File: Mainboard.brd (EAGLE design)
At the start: 162.6 x 52.1 mm, 77 parts, among them IC1 MS5611-01BA03, IC2 MCP73831, Q1 BSS84, U1 LM2937IMP-3.3, U2 USD-SOCKETNEW

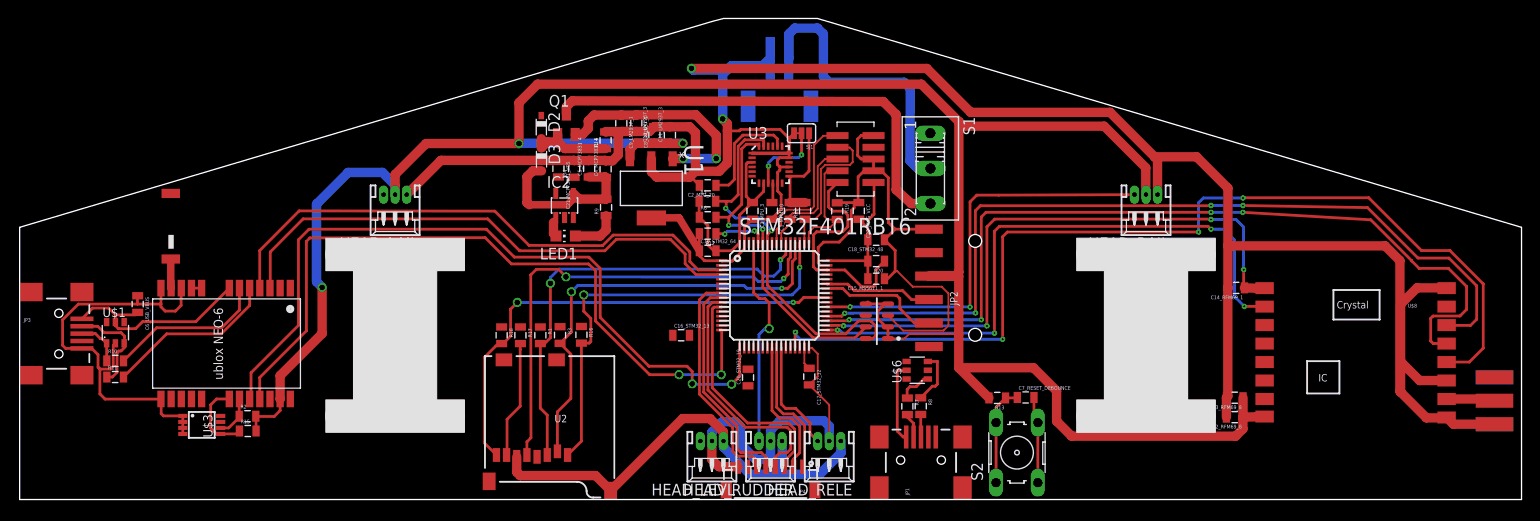
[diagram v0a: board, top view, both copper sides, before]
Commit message: Updated board wiring
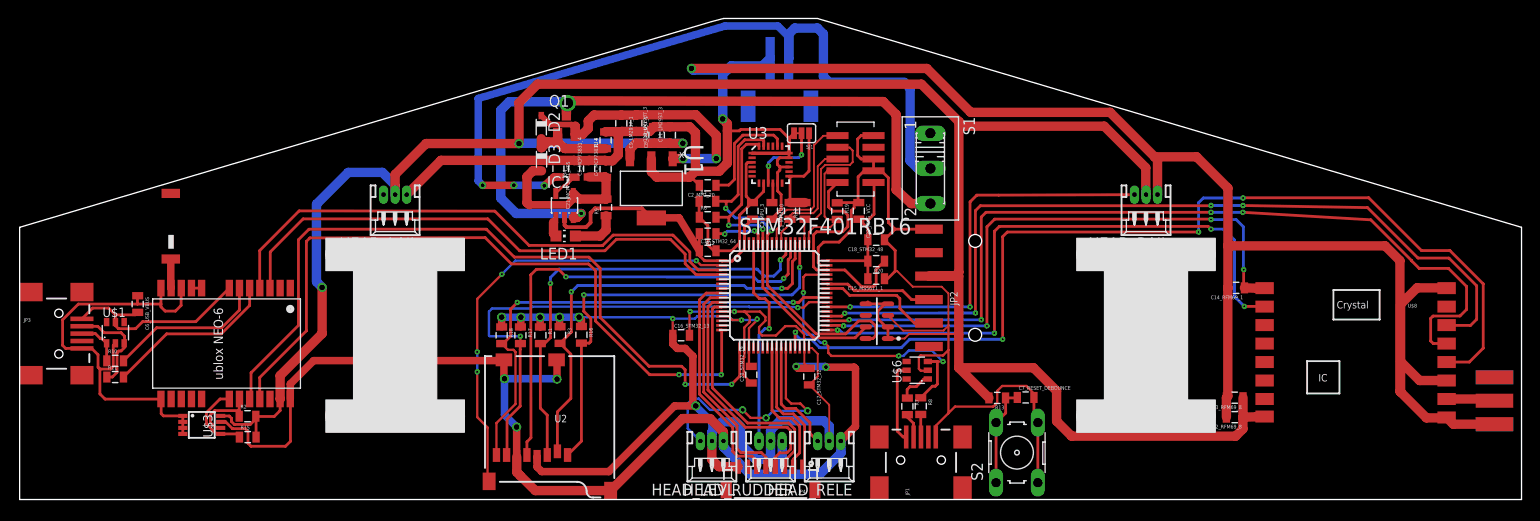
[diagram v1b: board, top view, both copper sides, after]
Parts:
- moved R15 0.66 mm to (24.7, 19.5)
- moved C20_STM32_19 0.47 mm to (79.2, 26.2)
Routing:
- net GND: track 451.9 -> 600.2 mm, vias 2 -> 9
- net VDD: track 346.4 -> 429.7 mm, vias 3 -> 12
- net N$2: track 31.8 -> 89.5 mm, vias 0 -> 3
- net SD_DETECT: track 0.00 -> 48.7 mm, vias 0 -> 4
- net SDIO_D0: track 13.0 -> 56.9 mm, vias 0 -> 2
- net +4.1V: track 49.8 -> 77.5 mm, vias 0 -> 2
- net USB_DP: track 5.90 -> 33.4 mm, vias 0 -> 4
- net TIM3_CH4: track 0.00 -> 27.4 mm, vias 0 -> 3
- net N$13: track 24.8 -> 29.9 mm
- net GPS_SCL: track 4.49 -> 7.37 mm
- net N$19: track 0.00 -> 2.74 mm
- net RFM_SCK: track 106.8 -> 107.5 mm

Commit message: Routed all remaining air wires
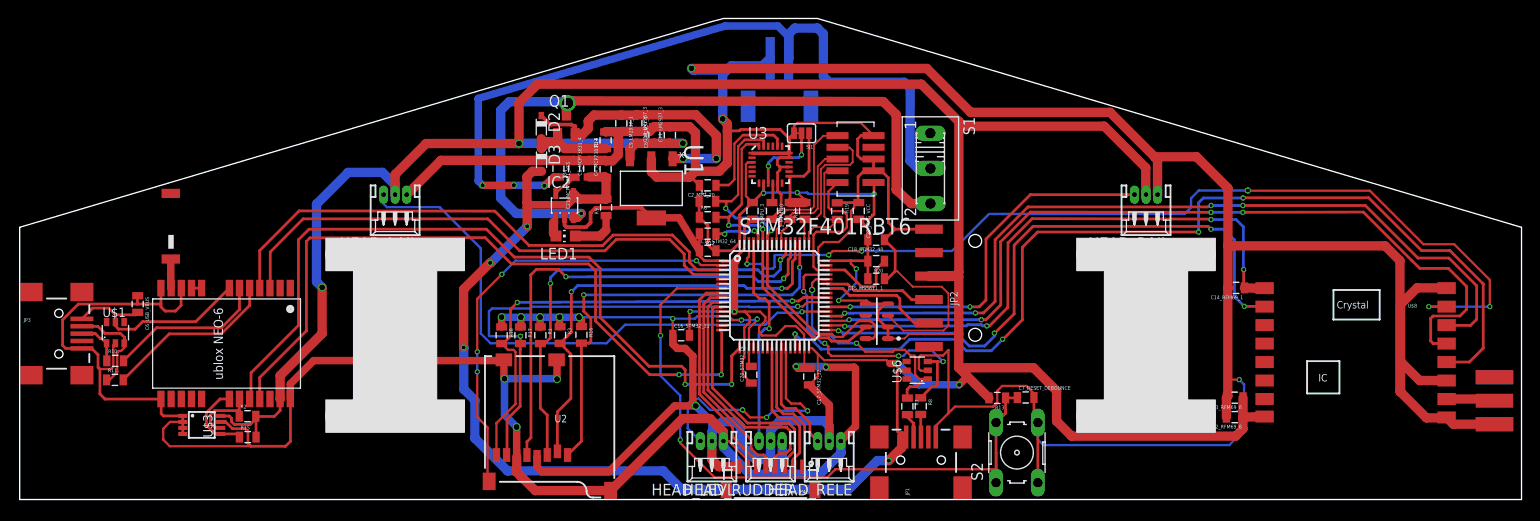
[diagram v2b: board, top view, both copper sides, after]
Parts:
- moved R11 0.31 mm to (10.3, 25.7)
- moved D3 0.05 mm to (56.5, 49.5)
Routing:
- net RFM_NSS: track 0.00 -> 103.2 mm, vias 0 -> 6
- net N$1: track 27.4 -> 116.7 mm, vias 0 -> 4
- net GND: track 600.2 -> 668.4 mm, vias 9 -> 10
- net NRST: track 10.9 -> 75.1 mm, vias 0 -> 2
- net TIM3_CH1: track 0.00 -> 62.1 mm, vias 0 -> 1
- net VDD: track 429.7 -> 472.4 mm, vias 12 -> 19
- net USB_DM: track 3.65 -> 26.4 mm, vias 0 -> 2
- net TIM3_CH2: track 45.0 -> 42.2 mm
- net RFM_MOSI: track 92.5 -> 89.9 mm
- net RFM_MISO: track 94.7 -> 92.5 mm
- net RFM_RST: track 65.4 -> 63.3 mm
- net RFM_SCK: track 107.5 -> 106.4 mm
- net ADC1_IN10: track 24.3 -> 23.3 mm
- net ADC1_IN11: track 23.9 -> 23.0 mm

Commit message: Fixed DRC errors
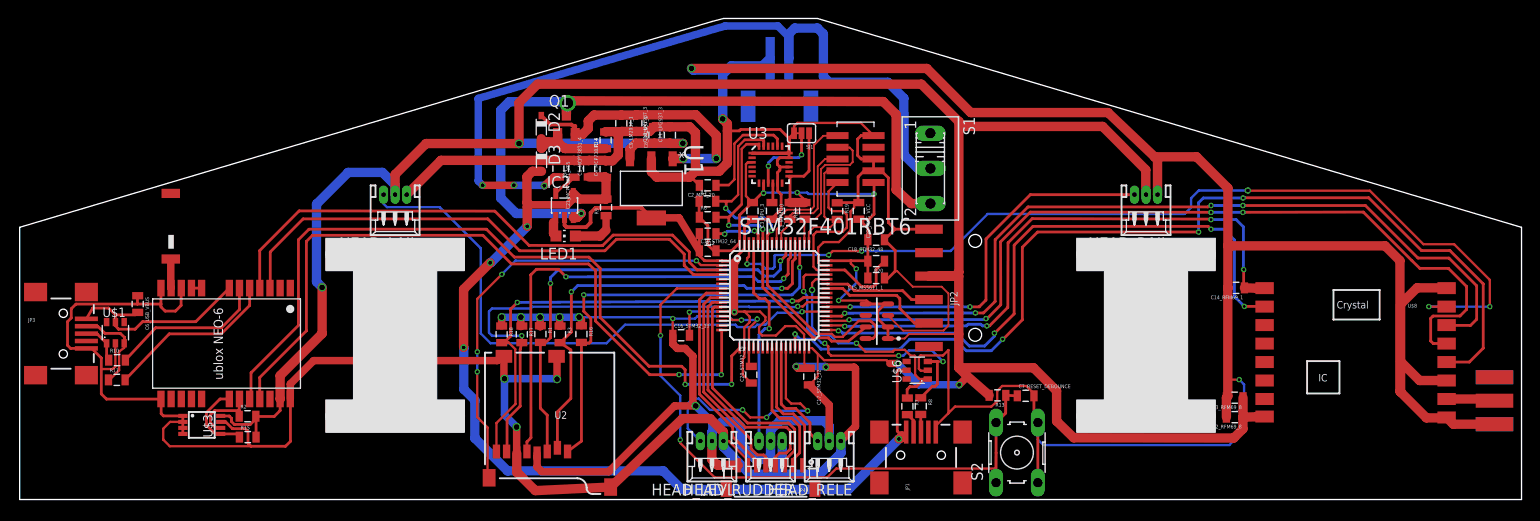
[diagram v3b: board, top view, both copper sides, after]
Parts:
- moved JP1 0.53 mm to (97.6, 17.5)
- moved JP3 0.48 mm to (4.72, 30.7)
- moved U2 0.38 mm to (50.4, 28.6)
- moved R13 0.28 mm to (105.8, 24.0)
- moved R10 0.22 mm to (10.5, 27.8)
- moved R11 0.20 mm to (10.5, 25.7)
- moved R17 0.18 mm to (54.4, 30.6)
- moved C7_RESET_DEBOUNCE 0.18 mm to (108.9, 23.9)
- moved JP4 0.15 mm to (81.3, 16.4)
- moved R1 0.13 mm to (56.4, 30.6)
- moved R18 0.10 mm to (52.2, 30.6)
- moved C15_MS5611_1 0.08 mm to (92.7, 36.7)
- moved R16 0.08 mm to (60.8, 30.6)
- moved R3 0.08 mm to (58.5, 30.6)
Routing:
- net N$2: track 89.5 -> 88.4 mm
- net N$17: track 2.70 -> 3.24 mm
- net SDIO_D0: track 56.9 -> 57.4 mm

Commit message: Fixed aileron slots
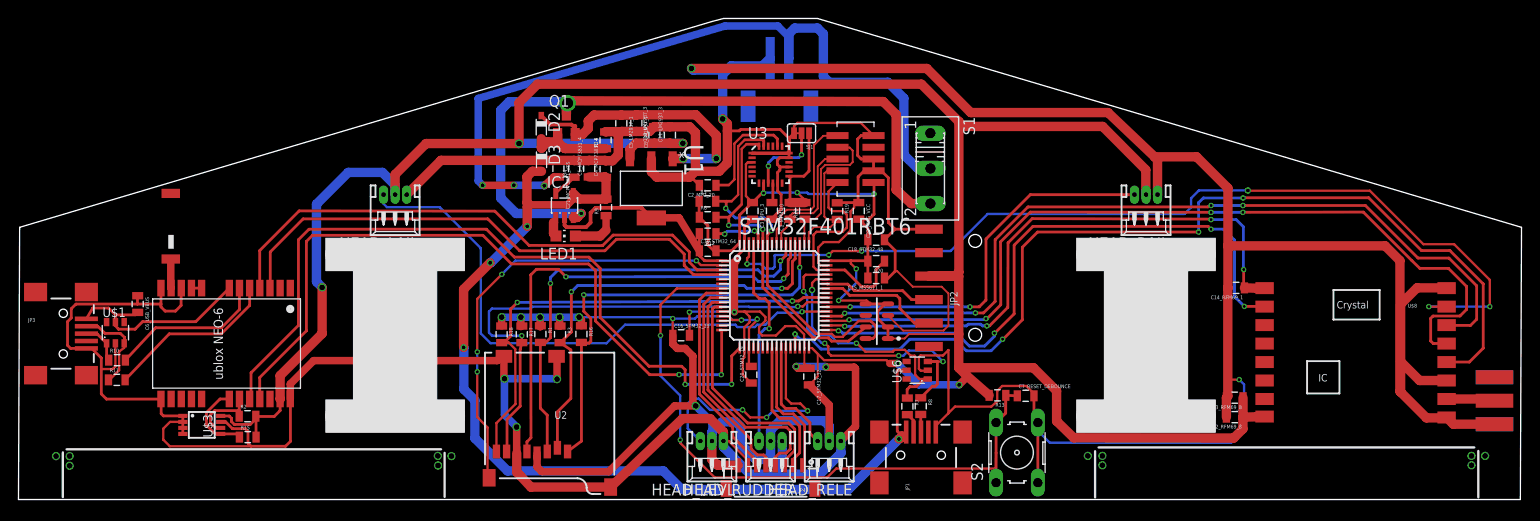
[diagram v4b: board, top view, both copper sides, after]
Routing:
- net GND: track 668.7 -> 667.8 mm
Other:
- board size 162.6 x 52.1 mm -> 162.7 x 52.1 mm
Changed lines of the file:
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@@
 <board>
 <plain>
-<wire x1="0" y1="12.7" x2="162.5654" y2="12.7" width="0" layer="20"/>
-<wire x1="162.5654" y1="12.7" x2="162.5654" y2="42.1642" width="0" layer="20"/>
+<wire x1="-0.127" y1="12.7" x2="162.4384" y2="12.7" width="0" layer="20"/>
+<wire x1="162.4384" y1="12.7" x2="162.5654" y2="42.1642" width="0" layer="20"/>
 <wire x1="162.5654" y1="42.1642" x2="86.36" y2="64.77" width="0" layer="20"/>
 <wire x1="86.36" y1="64.77" x2="76.2" y2="64.77" width="0" layer="20"/>
 <wire x1="76.2" y1="64.77" x2="74.93" y2="64.44" width="0" layer="20"/>
 <wire x1="74.93" y1="64.44" x2="0" y2="42.1642" width="0" layer="20"/>
-<wire x1="0" y1="42.1642" x2="0" y2="12.7" width="0" layer="20"/>
-<polygon width="0.3048" layer="39">
-<vertex x="0.1524" y="12.7"/>
-<vertex x="49.022" y="12.7"/>
-<vertex x="48.9712" y="17.78"/>
-<vertex x="0.1524" y="17.78"/>
-</polygon>
-<polygon width="0.3048" layer="39">
-<vertex x="113.4618" y="12.827"/>
-<vertex x="162.3314" y="12.827"/>
-<vertex x="162.2806" y="17.907"/>
-<vertex x="113.4618" y="17.907"/>
-</polygon>
+<wire x1="0" y1="42.1642" x2="-0.127" y2="12.7" width="0" layer="20"/>
+<wire x1="4.6736" y1="12.954" x2="4.6736" y2="17.8054" width="0.254" layer="21"/>
+<wire x1="5.08" y1="18.1356" x2="45.6184" y2="18.1356" width="0.254" layer="21"/>
+<wire x1="45.9994" y1="12.9794" x2="45.9994" y2="17.7546" width="0.254" layer="21"/>
+<wire x1="116.4082" y1="12.9286" x2="116.4082" y2="17.9324" width="0.254" layer="21"/>
+<wire x1="116.7892" y1="18.3388" x2="157.4546" y2="18.3388" width="0.254" layer="21"/>
+<wire x1="157.8864" y1="12.9286" x2="157.8864" y2="17.9578" width="0.254" layer="21"/>
 </plain>
 <attributes>
@@
 <wire x1="74.7268" y1="21.463" x2="76.18" y2="20.0098" width="1.016" layer="1"/>
 <wire x1="76.18" y1="20.0098" x2="76.18" y2="19.03" width="1.016" layer="1"/>
-<wire x1="63.9682" y1="14.0504" x2="55.819" y2="13.6652" width="1.016" layer="1"/>
-<wire x1="55.819" y1="13.6652" x2="54.1782" y2="15.2908" width="1.016" layer="1"/>
+<wire x1="63.9682" y1="14.0504" x2="55.3364" y2="14.0462" width="1.016" layer="1"/>
+<wire x1="55.3364" y1="14.0462" x2="54.1782" y2="15.2908" width="1.016" layer="1"/>
 <wire x1="54.1782" y1="15.2908" x2="53.8082" y2="15.6608" width="1.016" layer="1"/>
 <wire x1="53.8082" y1="15.6608" x2="53.8082" y2="17.7004" width="1.016" layer="1"/>
@@
 <wire x1="132.0038" y1="25.6794" x2="132.5372" y2="25.146" width="0.254" layer="16"/>
 <wire x1="132.5372" y1="25.146" x2="132.5372" y2="20.193" width="0.254" layer="16"/>
-<wire x1="132.5372" y1="20.193" x2="130.937" y2="18.5928" width="0.254" layer="16"/>
-<wire x1="130.937" y1="18.5928" x2="110.8202" y2="18.5928" width="0.254" layer="16"/>
-<wire x1="110.8202" y1="18.5928" x2="110.2106" y2="19.2024" width="0.254" layer="16"/>
-<wire x1="110.2106" y1="19.2024" x2="110.2106" y2="21.0312" width="0.254" layer="16"/>
+<wire x1="132.5372" y1="20.193" x2="131.1402" y2="18.8468" width="0.254" layer="16"/>
+<wire x1="131.1402" y1="18.8468" x2="111.506" y2="18.8468" width="0.254" layer="16"/>
+<wire x1="111.506" y1="18.8468" x2="110.2106" y2="20.1422" width="0.254" layer="16"/>
+<wire x1="110.2106" y1="20.1422" x2="110.2106" y2="21.0312" width="0.254" layer="16"/>
 <wire x1="17.6604" y1="21.1022" x2="17.6552" y2="21.1074" width="0.254" layer="1"/>
 <wire x1="17.6552" y1="21.1074" x2="16.2814" y2="21.1074" width="0.254" layer="1"/>
@@
 <signal name="N$4">
 </signal>
+<signal name="N$6">
+<via x="3.937" y="17.399" extent="1-16" drill="0.6"/>
+<via x="5.4102" y="17.399" extent="1-16" drill="0.6"/>
+<via x="5.4102" y="16.3576" extent="1-16" drill="0.6"/>
+</signal>
+<signal name="N$7">
+<via x="46.736" y="17.399" extent="1-16" drill="0.6"/>
+<via x="45.2628" y="17.4244" extent="1-16" drill="0.6"/>
+<via x="45.2882" y="16.383" extent="1-16" drill="0.6"/>
+</signal>
+<signal name="N$8">
+<via x="115.6208" y="17.4244" extent="1-16" drill="0.6"/>
+<via x="117.1956" y="17.4244" extent="1-16" drill="0.6"/>
+<via x="117.1956" y="16.4084" extent="1-16" drill="0.6"/>
+</signal>
+<signal name="N$9">
+<via x="158.623" y="17.4244" extent="1-16" drill="0.6"/>
+<via x="157.1498" y="17.4244" extent="1-16" drill="0.6"/>
+<via x="157.1498" y="16.4084" extent="1-16" drill="0.6"/>
+</signal>
 </signals>
